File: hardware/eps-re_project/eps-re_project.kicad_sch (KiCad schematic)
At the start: 14 parts, among them J1 533980471, J10 533980471, J11 533980471, J12 53398-0671, J13 53398-0671, J14 533980471, J2 533980471, J3 53398-0671, J4 533980471, J5 533980471, J6 533980471, J7 533980471, J8 53398-0671, J9 533980471

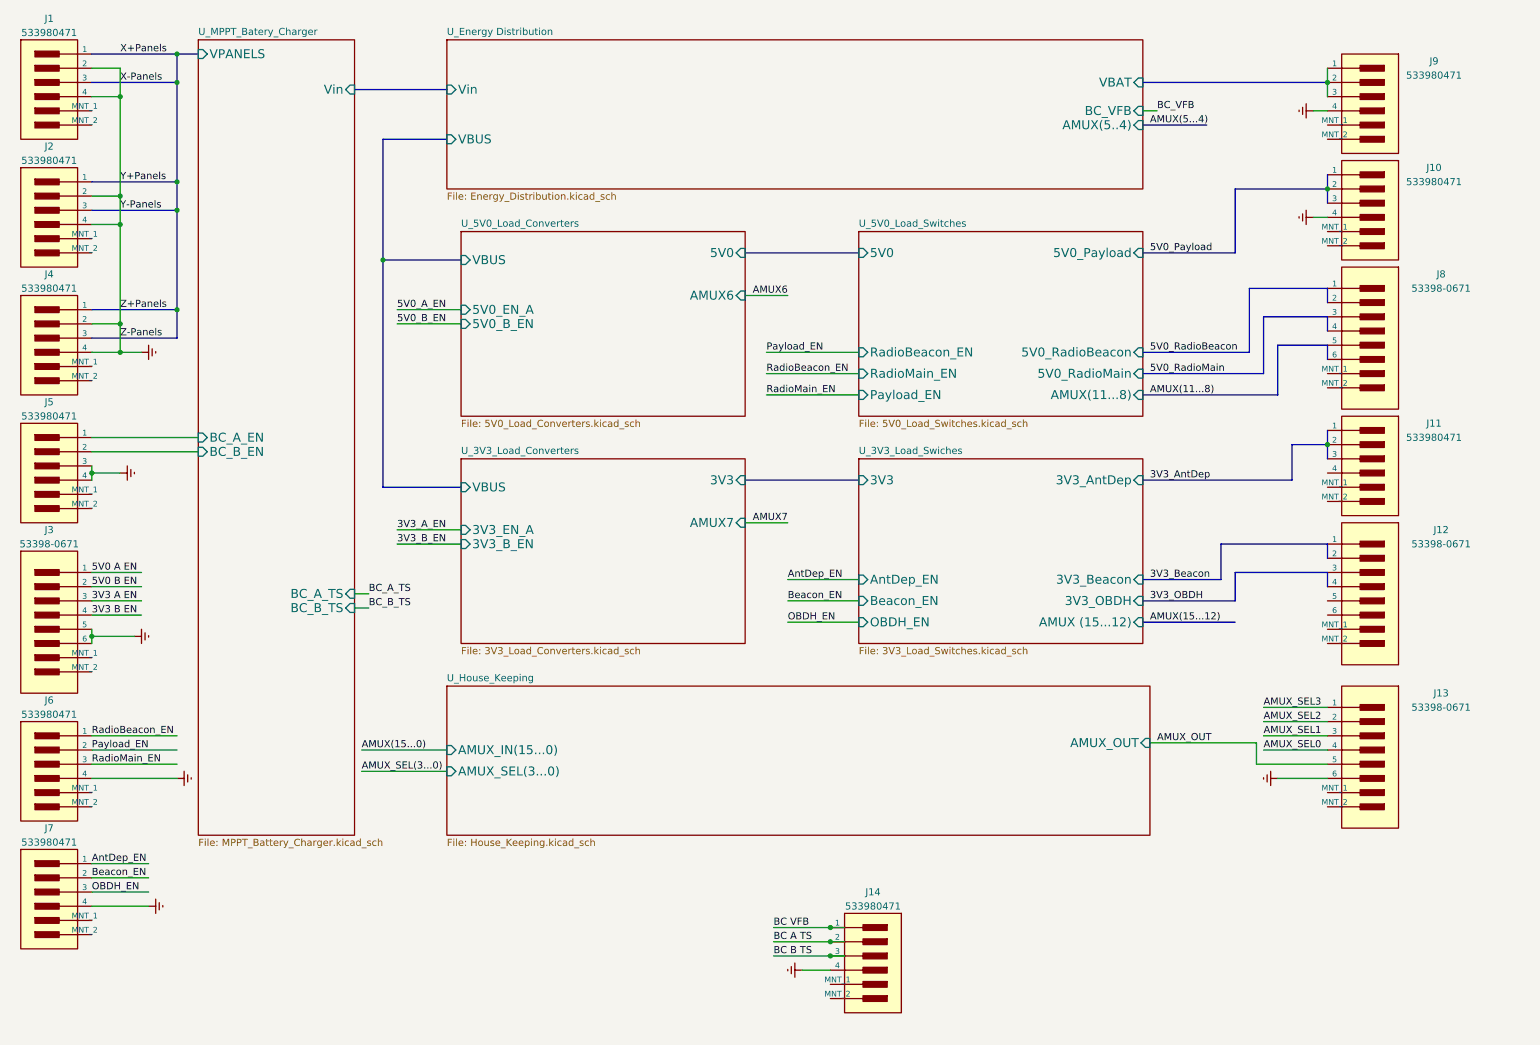
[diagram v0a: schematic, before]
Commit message: hardware: Restructuring the circuit, modifying symbols, footprints and other corrections
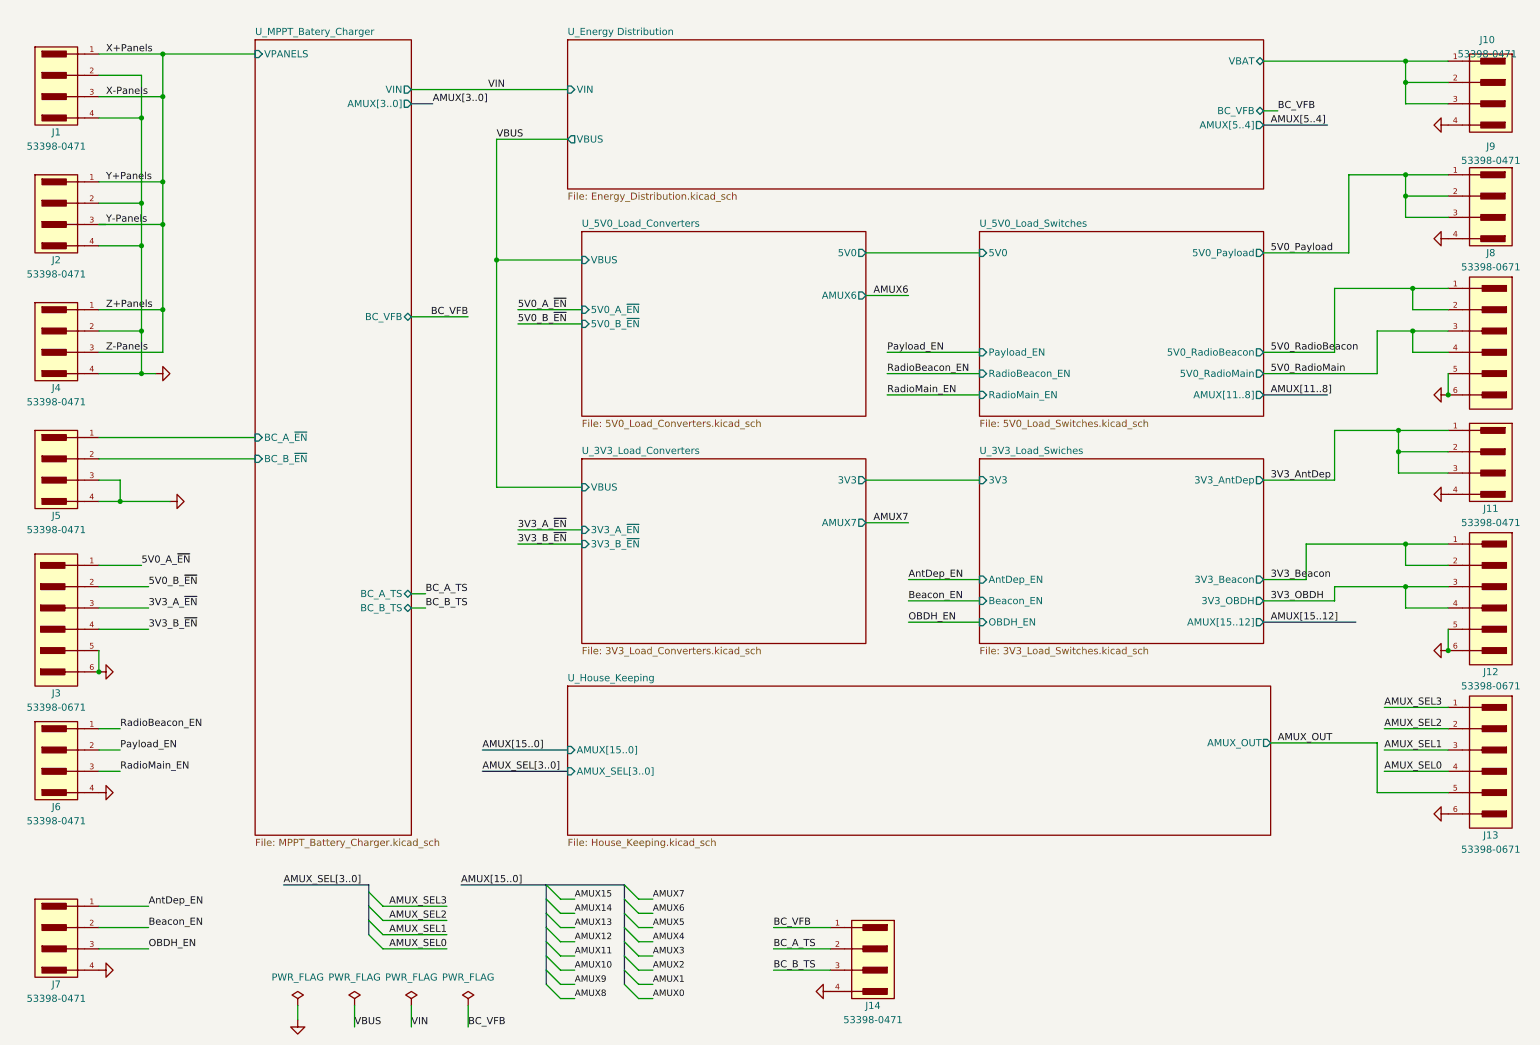
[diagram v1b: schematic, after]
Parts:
- removed J1, J10, J11, J14, J2, J4, J5, J6, J7, J9: 533980471, Molex-533980471-*, symbol 533980471:533980471
- added J1, J10, J11, J14, J2, J4, J5, J6, J7, J9: 53398-0471, footprints:533980471, symbol 533980471:533980471_1
- J12, J13, J3, J8: footprint Molex-53398-0671-0-0-* -> footprints:533980671
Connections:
- net 3V3_AntDep: now also J11.1, J11.2, J11.3
- net 3V3_Beacon: now also J12.1, J12.2
- net 3V3_OBDH: now also J12.3, J12.4
- net 5V0_Payload: now also J9.1, J9.2, J9.3
- net 5V0_RadioBeacon: now also J8.1, J8.2
- net 5V0_RadioMain: now also J8.3, J8.4
- net AMUX_OUT: now also J13.5; no longer J13. (MNT_2)
- net AMUX_SEL0: now also J13.4; no longer J13. (MNT_2)
- net AMUX_SEL1: now also J13.3; no longer J13. (MNT_2)
- net AMUX_SEL2: now also J13.2; no longer J13. (MNT_2)
- net AMUX_SEL3: now also J13.1; no longer J13. (MNT_2)
- net AntDep_EN: now also J7.1
- net BC_A_TS: now also J14.2
- net BC_B_TS: now also J14.3
- net BC_VFB: now also J14.1
- net Beacon_EN: now also J7.2
- net OBDH_EN: now also J7.3
- net Payload_EN: now also J6.2
- net RadioBeacon_EN: now also J6.1
- net RadioMain_EN: now also J6.3
- net U_Energy Distribution/VBAT: now also J10.1, J10.2, J10.3
- net X+Panels: now also J1.1, J1.3, J2.1, J2.3, J4.1, J4.3
- removed net 3V3 A EN: J3. (MNT_2)
- removed net 3V3 B EN: J3. (MNT_2)
- removed net 5V0 A EN: J3. (MNT_2)
- removed net 5V0 B EN: J3. (MNT_2)
- removed net Earth: J13. (MNT_2), J3. (MNT_2)
- new net 3V3_A_~{EN}: J3.3
- new net 3V3_B_~{EN}: J3.4
- new net 5V0_A_~{EN}: J3.1
- new net 5V0_B_~{EN}: J3.2
- new net GND: J1.2, J1.4, J10.4, J11.4, J12.5, J12.6, J13.6, J14.4, J2.2, J2.4, J3.5, J3.6, J4.2, J4.4, J5.3, J5.4, J6.4, J7.4, J8.5, J8.6, J9.4
- new net U_MPPT_Batery_Charger/BC_A_~{EN}: J5.1
- new net U_MPPT_Batery_Charger/BC_B_~{EN}: J5.2
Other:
- sheet U_3V3_Load_Converters ports: added 3V3_A_~{EN}, 3V3_B_~{EN}; removed 3V3_B_EN, 3V3_EN_A
- sheet U_3V3_Load_Swiches ports: added AMUX[15..12]; removed AMUX (15...12)
- sheet U_5V0_Load_Converters ports: added 5V0_A_~{EN}, 5V0_B_~{EN}; removed 5V0_B_EN, 5V0_EN_A
- sheet U_5V0_Load_Switches ports: added AMUX[11..8]; removed AMUX(11...8)
- sheet U_Energy Distribution ports: added AMUX[5..4], VIN; removed AMUX(5..4), Vin
- sheet U_House_Keeping ports: added AMUX[15..0], AMUX_SEL[3..0]; removed AMUX_IN(15...0), AMUX_SEL(3...0)
- sheet U_MPPT_Batery_Charger ports: added AMUX[3..0], BC_A_~{EN}, BC_B_~{EN}, BC_VFB, VIN; removed BC_A_EN, BC_B_EN, Vin
